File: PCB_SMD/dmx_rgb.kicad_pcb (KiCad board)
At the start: 2 copper layers, 52.1 x 42.9 mm, 30 parts, among them J1 CONN_01X02, J2 Conn_02x04_Odd_Even, J3 Conn_02x03_Odd_Even, J4 CONN_01X03, J5 CONN_01X04, J6 CONN_01X04, Q1 Q_NMOS_GSD, Q2 Q_NMOS_GSD, Q3 Q_NMOS_GSD, U1 ATTINY2313-20PU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

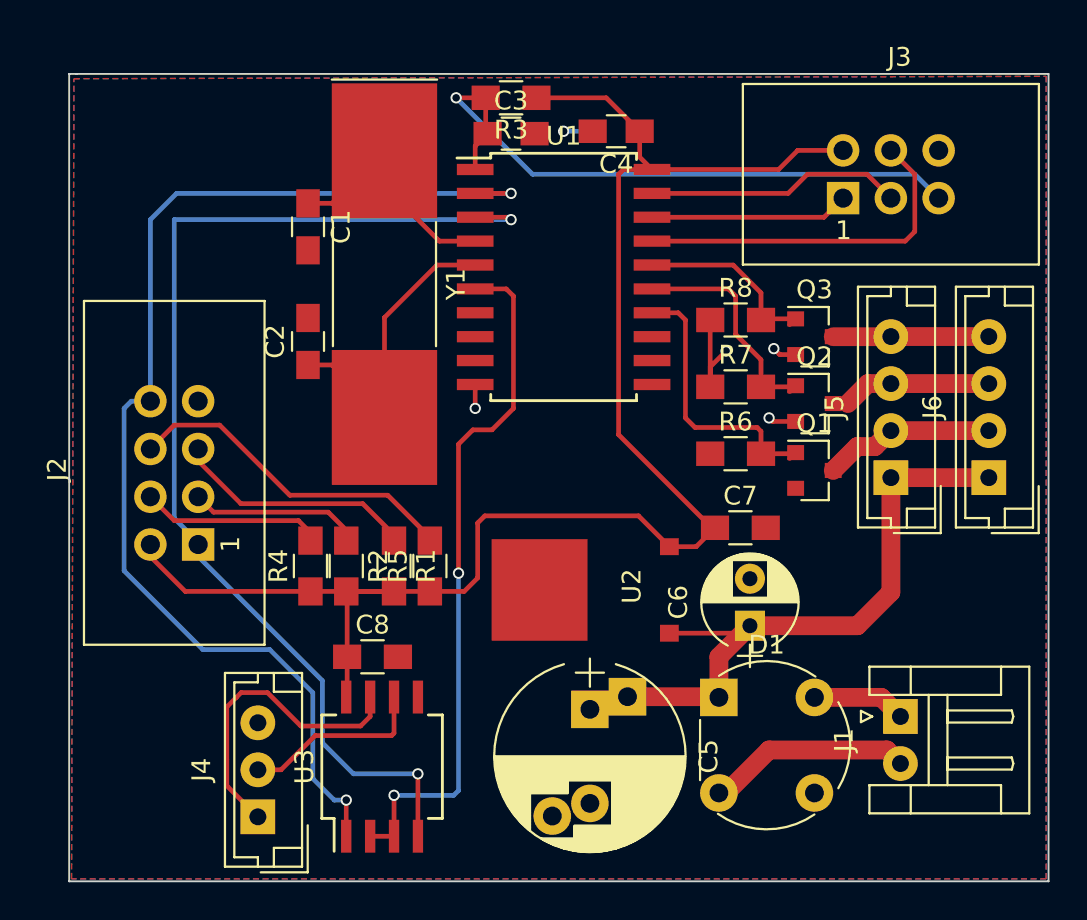
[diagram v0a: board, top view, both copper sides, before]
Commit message: spannungs wandler getauscht
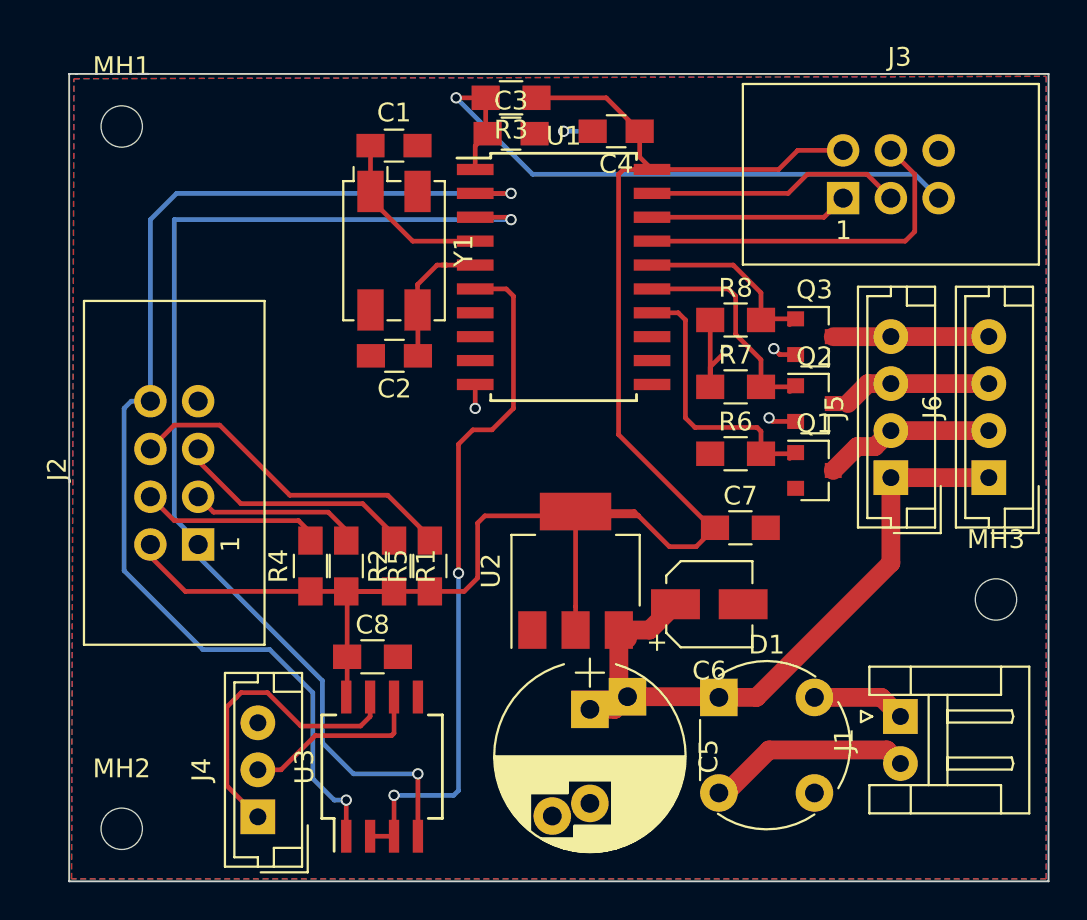
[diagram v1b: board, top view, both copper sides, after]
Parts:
- added MH1: MountingHole, Mounting_Holes:MountingHole_2.2mm_M2, F.Cu at (124.0, 19.3)
- added MH2: MountingHole, Mounting_Holes:MountingHole_2.2mm_M2, F.Cu at (124.0, 56.6)
- added MH3: MountingHole, Mounting_Holes:MountingHole_2.2mm_M2, F.Cu at (170.4, 44.5)
- C6: footprint Capacitors_THT:CP_Radial_D5.0mm_P2.50mm -> Capacitors_SMD:CP_Elec_4x5.8
- U2: value L7805 -> LM1117-3.3; footprint DPAK:DPAK -> TO_SOT_Packages_SMD:SOT-223-3Lead_TabPin2
- Y1: value Crystal -> Crystal_GND24; footprint Crystals:Crystal_SMD_SeikoEpson_MA505-2pin_12.7x5.1mm_HandSoldering -> Crystals:Crystal_SMD_EuroQuartz_MQ-4pin_7.0x5.0mm
- moved U2 7.06 mm to (148.1, 42.9)
- moved C1 6.29 mm to (138.4, 20.3), turned to 0 degrees
- moved C2 4.65 mm to (138.4, 31.5), turned to 180 degrees
- moved C6 2.44 mm to (155.2, 44.7), turned to 0 degrees
- moved Y1 1.85 mm to (138.4, 25.9)
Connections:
- U2 pad 1: +12V -> GND
- U2 pad 2: GND -> VCC
- U2 pad 3: VCC -> +12V
- Y1 pad 2: Net-(C2-Pad1) -> GND
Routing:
- net VCC: track 86.1 -> 95.8 mm
- net Net-(C2-Pad1): track 16.5 -> 7.55 mm
- net Net-(C1-Pad1): track 13.1 -> 9.33 mm
- net +12V: track 33.3 -> 37.0 mm

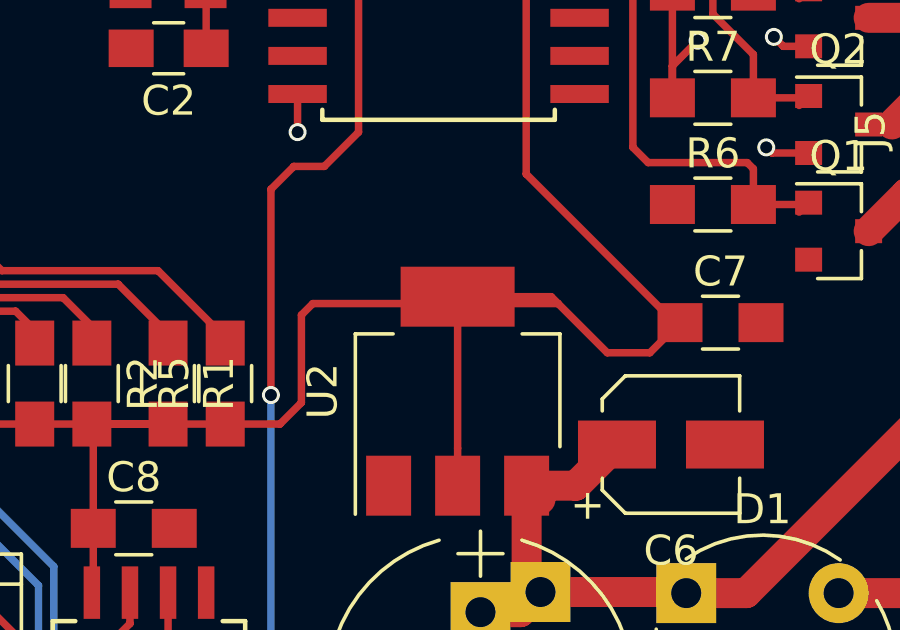
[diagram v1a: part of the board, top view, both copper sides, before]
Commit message: node red mqtt json upgrade
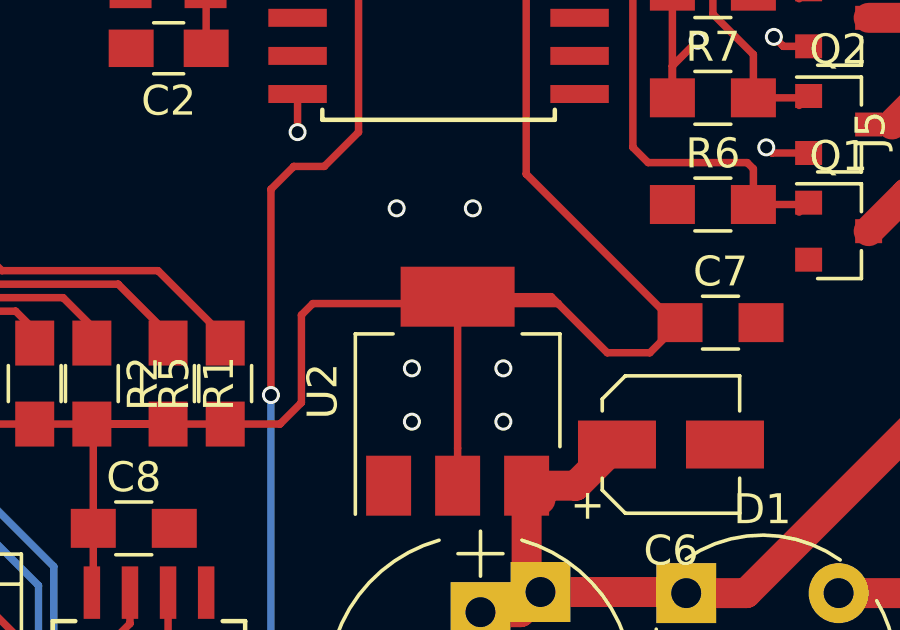
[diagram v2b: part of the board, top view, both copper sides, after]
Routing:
- net GND: vias 5 -> 11
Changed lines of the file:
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@@
     (thickness 1.6)
     (drawings 5)
-    (tracks 215)
+    (tracks 221)
     (zones 0)
     (modules 33)
@@
   (segment (start 137.2 29.078) (end 137.18 29.058) (width 0.25) (layer F.Cu) (net 2))
   (segment (start 137.18 28.658) (end 137.18 29.058) (width 0.25) (layer F.Cu) (net 2))
+  (via (at 149.606 42.164) (size 0.6) (drill 0.4) (layers F.Cu B.Cu) (net 2))
+  (via (at 149.606 43.942) (size 0.6) (drill 0.4) (layers F.Cu B.Cu) (net 2))
+  (via (at 146.558 43.942) (size 0.6) (drill 0.4) (layers F.Cu B.Cu) (net 2))
+  (via (at 146.558 42.164) (size 0.6) (drill 0.4) (layers F.Cu B.Cu) (net 2))
+  (via (at 146.05 36.83) (size 0.6) (drill 0.4) (layers F.Cu B.Cu) (net 2))
+  (via (at 148.59 36.83) (size 0.6) (drill 0.4) (layers F.Cu B.Cu) (net 2))
   (segment (start 139.7 29.078) (end 139.68 29.058) (width 0.25) (layer F.Cu) (net 3))
   (segment (start 139.7 31.496) (end 139.7 29.078) (width 0.25) (layer F.Cu) (net 3))
